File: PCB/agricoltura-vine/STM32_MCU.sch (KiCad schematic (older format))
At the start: 33 parts, among them SW1 TL3301NF260QG, T1 BU2032SM-JJ-GTR, T2 20021121-00010C4LF, T3 0675031020, U1 STM32F446RET6, X1 ABM3B-8.000MHZ-B2-T, X2 ABS07-32.768KHZ-9-T

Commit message: Majopr Progress
Board shape enlarged to simplify layout and accomodate larger size parts for sisterboard like Ivy. QWIIC connectors flipped to be correct, signals were oriented incorrectly in past revisions.
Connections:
- net labels added: 5VGPIO_BD_0, 5VGPIO_BD_1, 5VGPIO_BD_2, 5VGPIO_BD_3, 5VGPIO_BD_4, 5VGPIO_BD_5, 5VGPIO_BD_6, 5VGPIO_BD_7
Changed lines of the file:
@@
 Text HLabel 1200 3750 0    50   Input ~ 0
 UART_SENSE1_RX
-Wire Wire Line
-	1200 3650 4800 3650
 $Comp
 L AVR-KiCAD-Lib-Capacitors:C0402C104K9PACTU C5
@@
 Wire Wire Line
 	6650 2550 10500 2550
+Text HLabel 2100 2400 0    50   Input ~ 0
+5VGPIO_BD_0
+Text HLabel 2100 2500 0    50   Input ~ 0
+5VGPIO_BD_1
+Text HLabel 2100 2600 0    50   Input ~ 0
+5VGPIO_BD_2
+Text HLabel 2100 2700 0    50   Input ~ 0
+5VGPIO_BD_3
+Text HLabel 2100 2800 0    50   Input ~ 0
+5VGPIO_BD_4
+Text HLabel 2100 2900 0    50   Input ~ 0
+5VGPIO_BD_5
+Text HLabel 2100 3000 0    50   Input ~ 0
+5VGPIO_BD_6
+Text HLabel 1200 3850 0    50   Input ~ 0
+5VGPIO_BD_7
+Wire Wire Line
+	4800 3850 1200 3850
 $EndSCHEMATC

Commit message: Big Update
Dropped 8 5V outputs in favor of two relays. Ditched microchip IO expander for a Ti one that does level conversion for outputs, eliminates Ti bidriectional converter and 74 line driver from design, simplifying everything.
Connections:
- net labels removed: 5VGPIO_BD_0, 5VGPIO_BD_1, 5VGPIO_BD_2, 5VGPIO_BD_3, 5VGPIO_BD_4, 5VGPIO_BD_5, 5VGPIO_BD_6
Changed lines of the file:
@@
 Wire Wire Line
 	4800 1850 1200 1850
-Text HLabel 6650 1750 2    50   Input ~ 0
+Text HLabel 6650 1550 2    50   Input ~ 0
 USW1_EN
 Text HLabel 6650 1650 2    50   Input ~ 0
 USW1_S0
-Text HLabel 6650 1550 2    50   Input ~ 0
+Text HLabel 6650 1750 2    50   Input ~ 0
 USW1_S1
 Text HLabel 1200 3750 0    50   Input ~ 0
@@
 Wire Wire Line
 	6650 2550 10500 2550
-Text HLabel 2100 2400 0    50   Input ~ 0
-5VGPIO_BD_0
-Text HLabel 2100 2500 0    50   Input ~ 0
-5VGPIO_BD_1
-Text HLabel 2100 2600 0    50   Input ~ 0
-5VGPIO_BD_2
-Text HLabel 2100 2700 0    50   Input ~ 0
-5VGPIO_BD_3
-Text HLabel 2100 2800 0    50   Input ~ 0
-5VGPIO_BD_4
-Text HLabel 2100 2900 0    50   Input ~ 0
-5VGPIO_BD_5
-Text HLabel 2100 3000 0    50   Input ~ 0
-5VGPIO_BD_6
 Text HLabel 1200 3850 0    50   Input ~ 0
 5VGPIO_BD_7

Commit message: Relay Driver Circuit, Board Size Change
Added the Relay driver circuitry, increased size of board tobetter acccomodate relays, figuredout the powerplane topology to get 5Vs where it needs to go.
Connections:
- net labels added: IO_INT_N, IO_RESET, IO_SCL, IO_SDA
- net labels removed: 5VGPIO_BD_7
- wire segments 128 -> 137
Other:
- moved on the sheet: C10, C11, R1, SW1

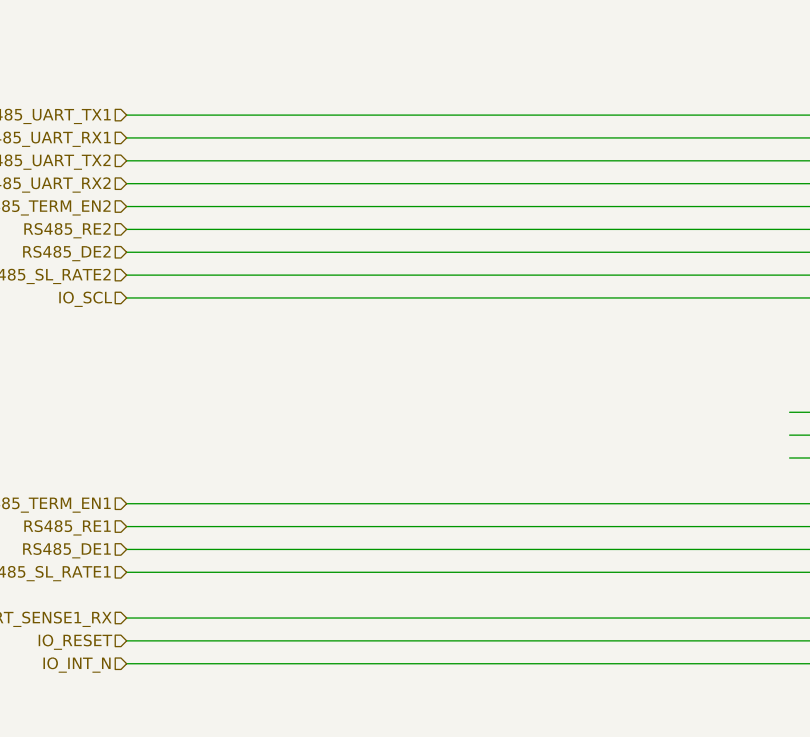
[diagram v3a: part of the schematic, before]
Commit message: Netlabels and Datasheets
Removed datasheets for parts no longer in design, added datasheet for RS485 transceiver. Added netlabels for RS485 signals.
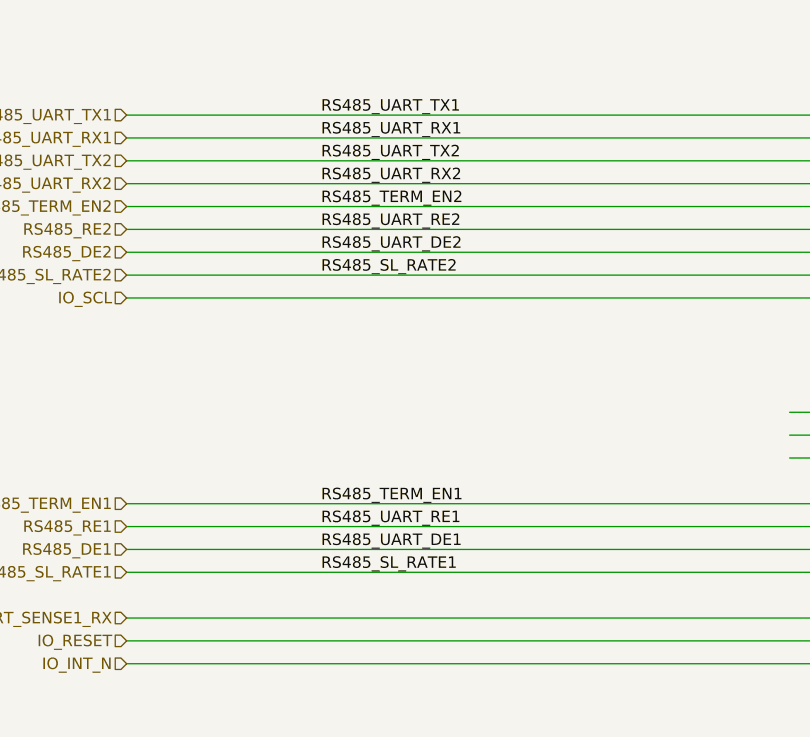
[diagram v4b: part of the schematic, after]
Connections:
- net labels added: RS485_UART_DE1, RS485_UART_DE2, RS485_UART_RE1, RS485_UART_RE2
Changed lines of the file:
@@
 Wire Wire Line
 	6100 5400 5950 5400
+Text Label 2050 1550 0    50   ~ 0
+RS485_UART_TX1
+Text Label 2050 3250 0    50   ~ 0
+RS485_TERM_EN1
+Text Label 2050 1650 0    50   ~ 0
+RS485_UART_RX1
+Text Label 2050 3550 0    50   ~ 0
+RS485_SL_RATE1
+Text Label 2050 3450 0    50   ~ 0
+RS485_UART_DE1
+Text Label 2050 3350 0    50   ~ 0
+RS485_UART_RE1
+Text Label 2050 1750 0    50   ~ 0
+RS485_UART_TX2
+Text Label 2050 1950 0    50   ~ 0
+RS485_TERM_EN2
+Text Label 2050 1850 0    50   ~ 0
+RS485_UART_RX2
+Text Label 2050 2250 0    50   ~ 0
+RS485_SL_RATE2
+Text Label 2050 2150 0    50   ~ 0
+RS485_UART_DE2
+Text Label 2050 2050 0    50   ~ 0
+RS485_UART_RE2
 $EndSCHEMATC

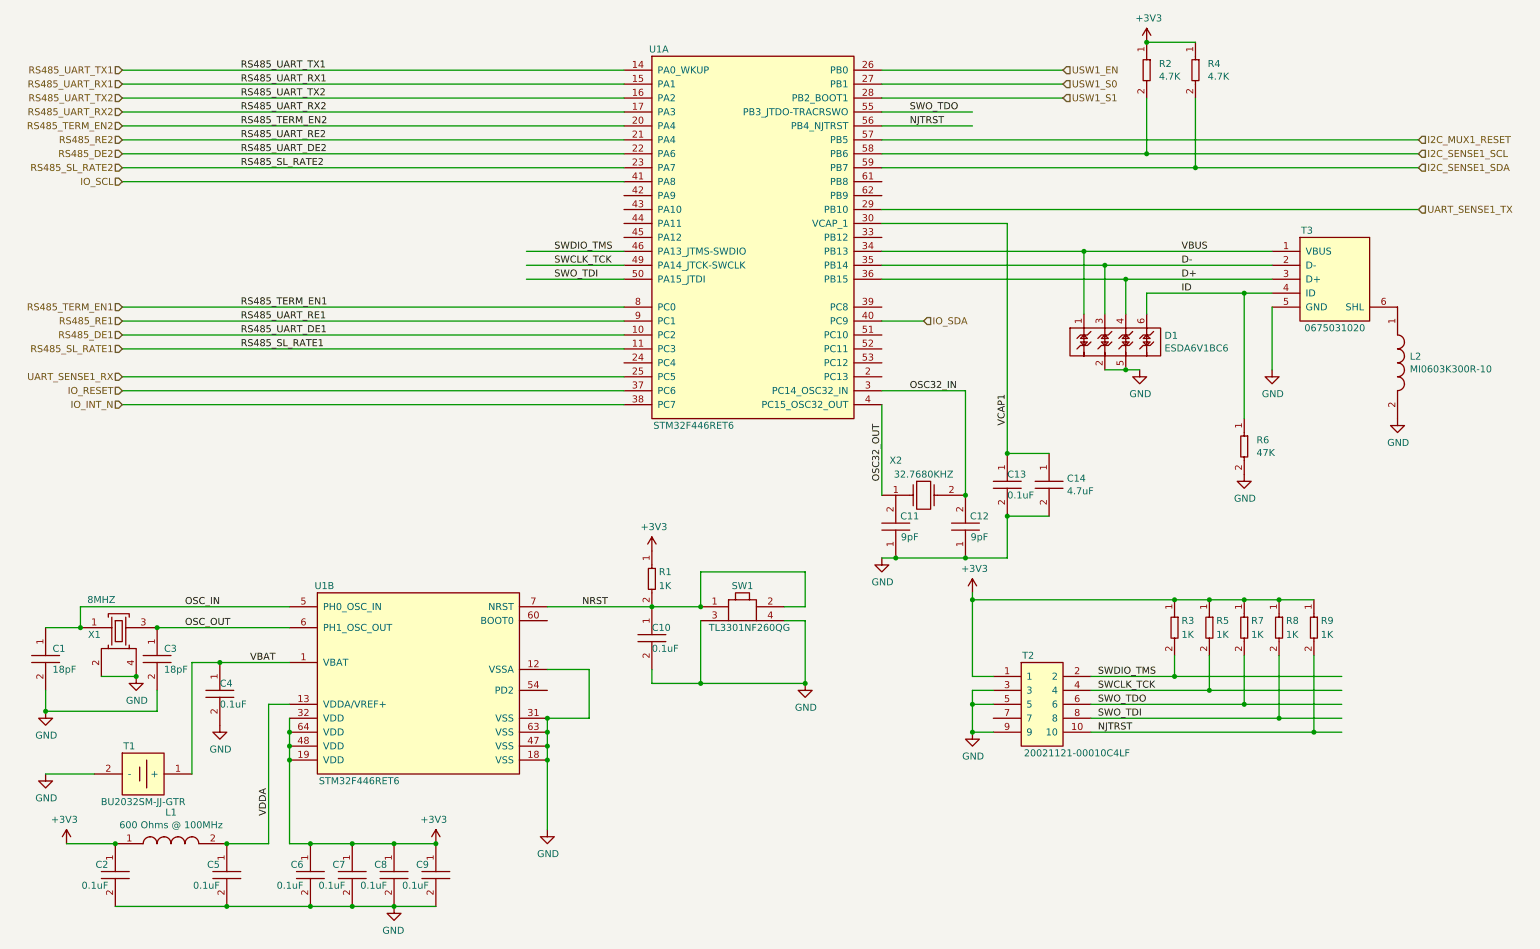
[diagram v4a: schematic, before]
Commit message: EEPROM
Added EEPROM chip to design, also beefed up USB grounding and shock protection
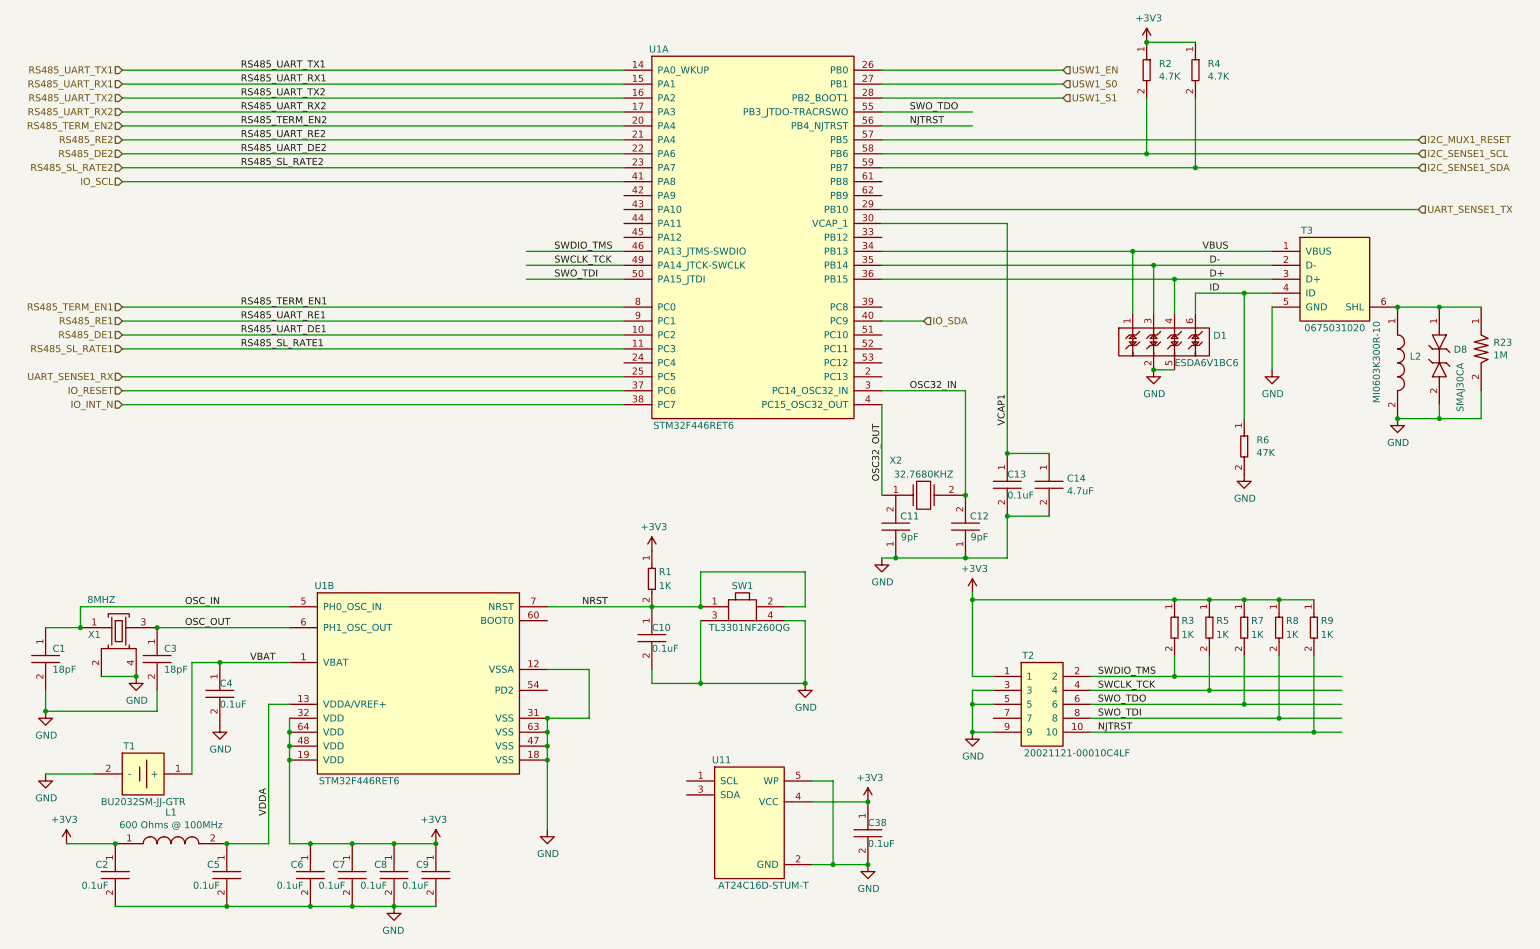
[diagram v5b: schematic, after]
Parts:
- added C38: C0402C104K9PACTU, AVR-KiCAD-Lib-Resistors:R0402, symbol AVR-KiCAD-Lib-Capacitors:C0402C104K9PACTU
- added D8: SMAJ30CA, AVR-KiCAD-Lib-Diodes:SMAJ30CA, symbol AVR-KiCAD-Lib-Diodes:SMAJ30CA
- added R23: RC1206FR-071ML, AVR-KiCAD-Lib-Resistors:R1206, symbol AVR-KiCAD-Lib-Resistors:RC1206FR-071ML
- added U11: AT24C16D-STUM-T, AVR-KiCAD-Lib-ICs:SOT-23-5, symbol AVR-KiCAD-Lib-ICs:AT24C16D-STUM-T
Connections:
- wire segments 137 -> 147
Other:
- moved on the sheet: D1

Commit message: Added EEProm
Eeprom added and routed in circuit board, USB resitors added. TVS diodes and pullups added to I2C ports not yet placed.
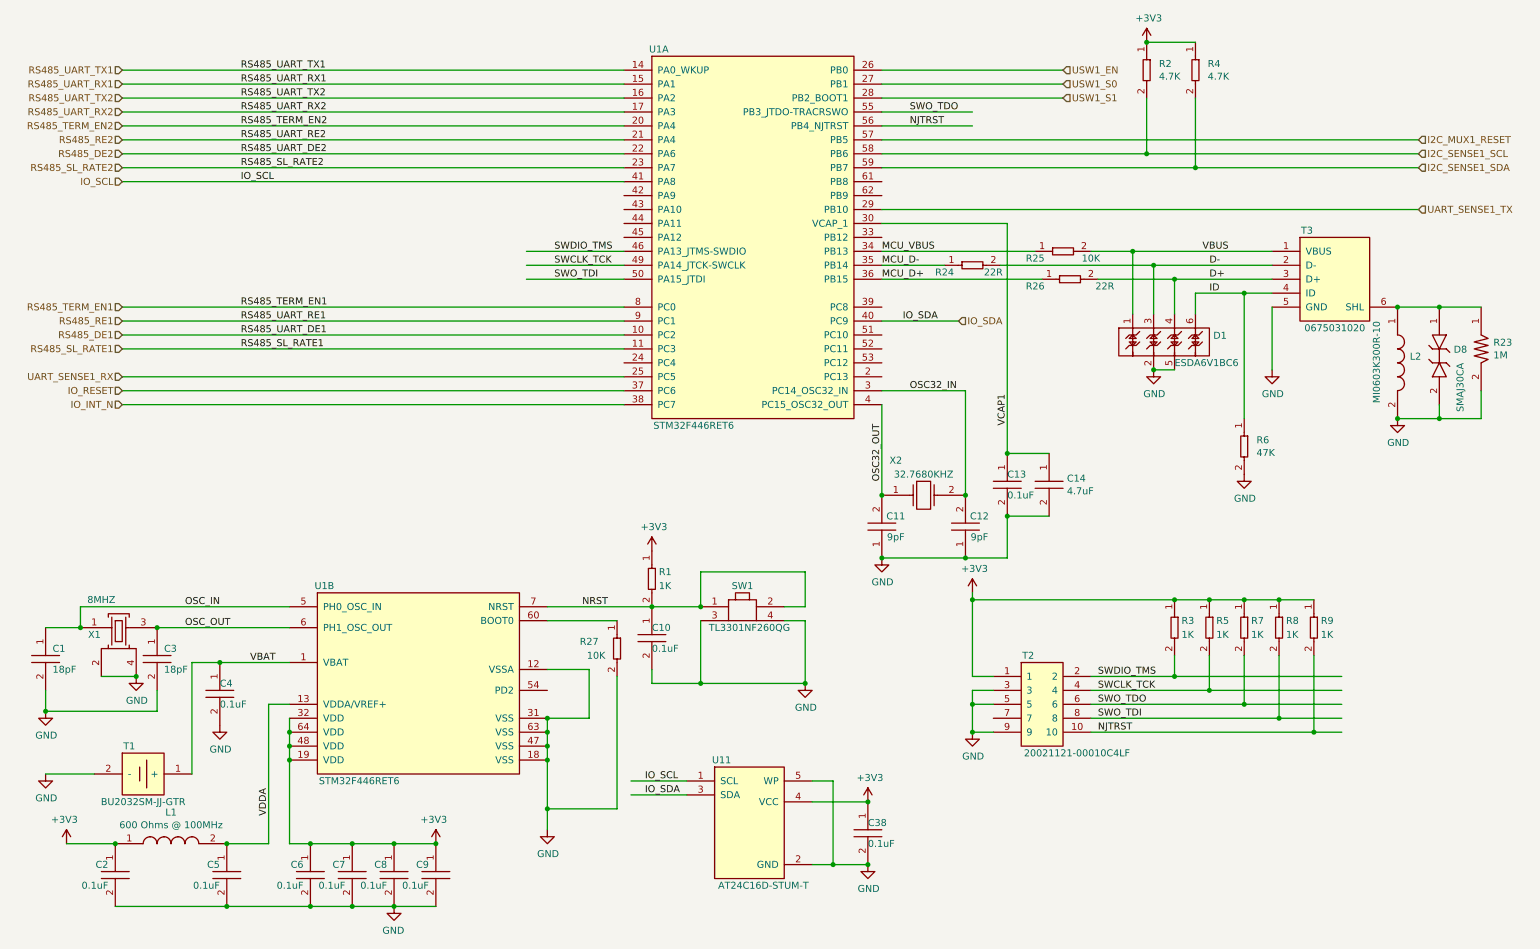
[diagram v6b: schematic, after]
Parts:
- added R24, R26: RC0402FR-0722RL, AVR-KiCAD-Lib-Resistors:R0402, symbol AVR-KiCAD-Lib-Resistors:RC0402FR-0722RL
- added R25, R27: RC0402FR-0710KL, AVR-KiCAD-Lib-Resistors:R0402, symbol AVR-KiCAD-Lib-Resistors:RC0402FR-0710KL
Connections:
- net labels added: MCU_D+, MCU_D-, MCU_VBUS
- wire segments 147 -> 155
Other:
- moved on the sheet: C11

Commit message: Board tweaks
TVS diodes added, board needs routing, a lot of board has been tweaked, more to come.
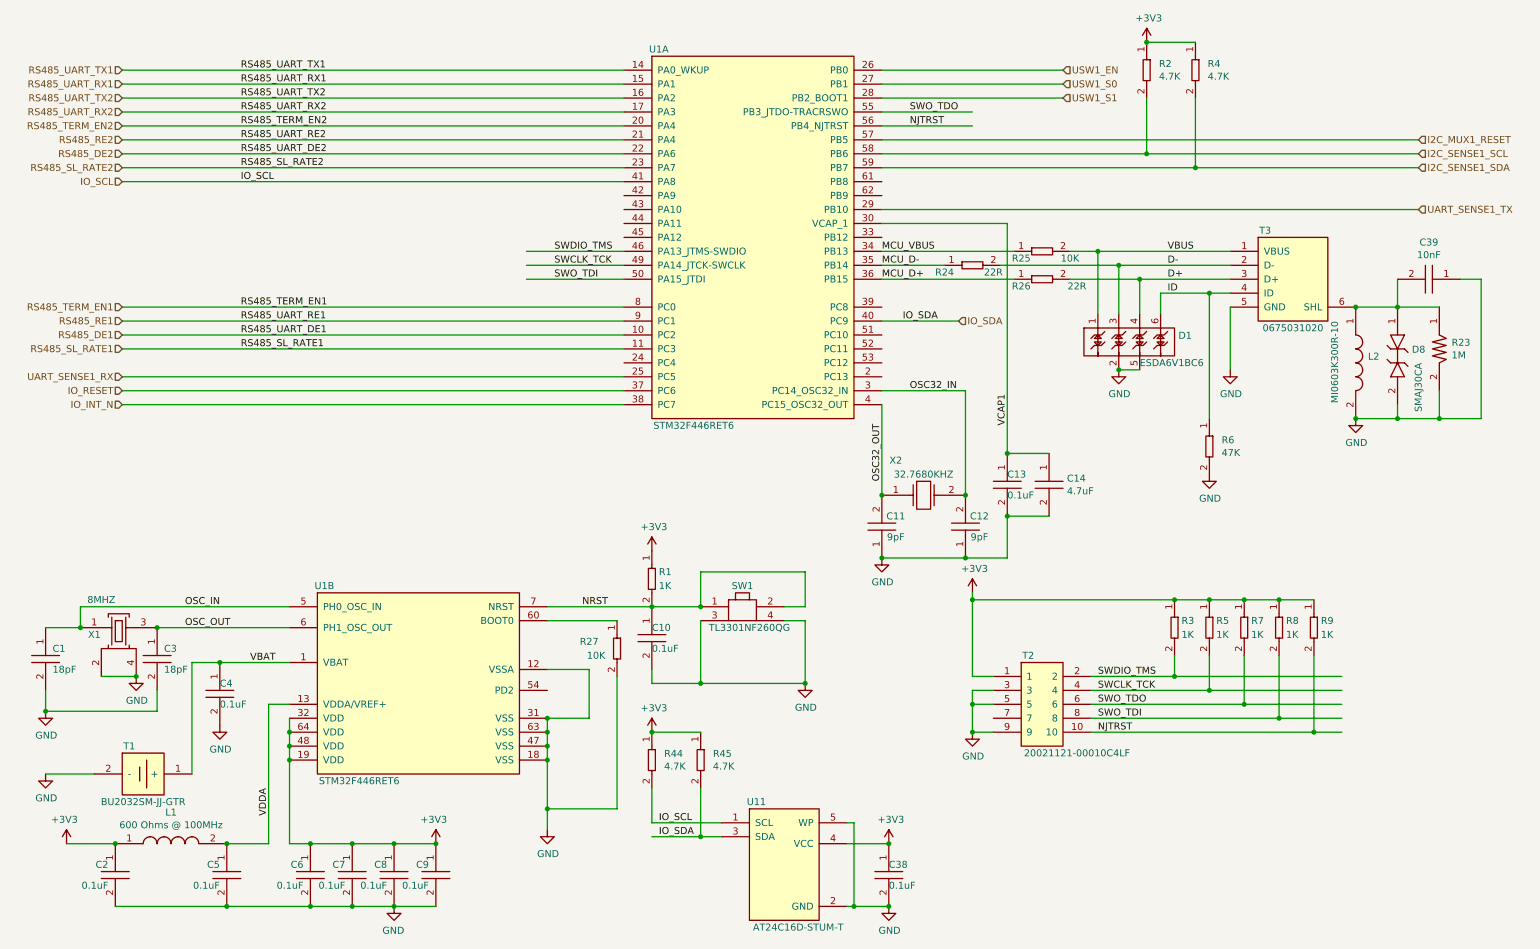
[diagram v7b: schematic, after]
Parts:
- added C39: C0603X103K1RAC3316, AVR-KiCAD-Lib-Capacitors:C0603, symbol AVR-KiCAD-Lib-Capacitors:C0603X103K1RAC3316
- added R44, R45: RC0402FR-074K7L, AVR-KiCAD-Lib-Resistors:R0402, symbol AVR-KiCAD-Lib-Resistors:RC0402FR-074K7L
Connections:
- wire segments 155 -> 163
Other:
- moved on the sheet: C38, D1, D8, L2, R23, R25, R26, R6, T3, U11
